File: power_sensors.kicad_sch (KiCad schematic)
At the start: 51 parts, among them U10 MCP6004, U11 MCP6004, U12 ZMPT101B, U13 ZMPT101B, U14 ZMPT101B, U15 JACK_PCB_3.5, U16 JACK_PCB_3.5, U17 JACK_PCB_3.5, U6 MLX91208, U7 MLX91208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

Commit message: Update 3d references and add testpoints
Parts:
- added TP3, TP4, TP5, TP6, TP7, TP8, TP9: (no value), symbol Connector:TestPoint
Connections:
- net 2V5: now also TP3.1
- net at R21.2, U10.10 (+), U14.4 (S1): now also TP6.1
- net at R20.2, U10.5 (+), U13.4 (S1): now also TP5.1
- net at R30.2, U11.10 (+), U17.1 (L)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: now also TP9.1
- net at R28.2, U11.3 (+), U15.1 (L)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: now also TP7.1
- net at R29.2, U11.5 (+), U16.1 (L)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: now also TP8.1
- net at R19.2, U10.3 (+), U12.4 (S1): now also TP4.1
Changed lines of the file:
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@@
   (junction (at 227.33 90.17) (diameter 0) (color 0 0 0 0)
   )
+  (junction (at 160.02 45.72) (diameter 0) (color 0 0 0 0)
+  )
   (junction (at 160.02 86.36) (diameter 0) (color 0 0 0 0)
   )
@@
   (junction (at 52.07 168.91) (diameter 0) (color 0 0 0 0)
   )
+  (junction (at 233.68 46.99) (diameter 0) (color 0 0 0 0)
+  )
   (junction (at 54.61 74.93) (diameter 0) (color 0 0 0 0)
   )
@@
   (junction (at 173.99 93.98) (diameter 0) (color 0 0 0 0)
   )
+  (junction (at 160.02 114.3) (diameter 0) (color 0 0 0 0)
+  )
   (junction (at 31.75 45.72) (diameter 0) (color 0 0 0 0)
   )
@@
   (junction (at 80.01 45.72) (diameter 0) (color 0 0 0 0)
   )
+  (junction (at 233.68 81.28) (diameter 0) (color 0 0 0 0)
+  )
   (junction (at 58.42 116.84) (diameter 0) (color 0 0 0 0)
+  )
+  (junction (at 160.02 80.01) (diameter 0) (color 0 0 0 0)
+  )
+  (junction (at 233.68 114.3) (diameter 0) (color 0 0 0 0)
   )
   (no_connect (at 140.97 177.8))
@@
     (pin "2")
   )
+  (symbol (lib_id "Connector:TestPoint") (at 233.68 114.3 0) (unit 1)
+    (in_bom yes) (on_board yes) (fields_autoplaced)
+    (property "Reference" "TP9" (id 0) (at 236.22 109.7279 0)
+      (effects (font (size 1.27 1.27)) (justify left))
+    )
+    (property "Value" "" (id 1) (at 236.22 112.2679 0)
+      (effects (font (size 1.27 1.27)) (justify left))
+    )
+    (property "Footprint" "" (id 2) (at 238.76 114.3 0)
+      (effects (font (size 1.27 1.27)) hide)
+    )
+    (property "Datasheet" "~" (id 3) (at 238.76 114.3 0)
+      (effects (font (size 1.27 1.27)) hide)
+    )
+    (pin "1")
+  )
   (symbol (lib_id "guille_library:JACK_PCB_3.5") (at 217.17 125.73 0) (unit 1)
     (in_bom yes) (on_board yes) (fields_autoplaced)
@@
     (pin "8")
   )
+  (symbol (lib_id "Connector:TestPoint") (at 160.02 45.72 0) (unit 1)
+    (in_bom yes) (on_board yes) (fields_autoplaced)
+    (property "Reference" "TP4" (id 0) (at 162.56 41.1479 0)
+      (effects (font (size 1.27 1.27)) (justify left))
+    )
+    (property "Value" "" (id 1) (at 162.56 43.6879 0)
+      (effects (font (size 1.27 1.27)) (justify left))
+    )
+    (property "Footprint" "" (id 2) (at 165.1 45.72 0)
+      (effects (font (size 1.27 1.27)) hide)
+    )
+    (property "Datasheet" "~" (id 3) (at 165.1 45.72 0)
+      (effects (font (size 1.27 1.27)) hide)
+    )
+    (pin "1")
+  )
   (symbol (lib_id "power:GND") (at 58.42 92.71 0) (unit 1)
     (in_bom yes) (on_board yes) (fields_autoplaced)
@@
     (pin "1")
     (pin "2")
+  )
+  (symbol (lib_id "Connector:TestPoint") (at 160.02 80.01 0) (unit 1)
+    (in_bom yes) (on_board yes) (fields_autoplaced)
+    (property "Reference" "TP5" (id 0) (at 162.56 75.4379 0)
+      (effects (font (size 1.27 1.27)) (justify left))
+    )
+    (property "Value" "" (id 1) (at 162.56 77.9779 0)
+      (effects (font (size 1.27 1.27)) (justify left))
+    )
+    (property "Footprint" "" (id 2) (at 165.1 80.01 0)
+      (effects (font (size 1.27 1.27)) hide)
+    )
+    (property "Datasheet" "~" (id 3) (at 165.1 80.01 0)
+      (effects (font (size 1.27 1.27)) hide)
+    )
+    (pin "1")
   )
   (symbol (lib_id "Device:R") (at 133.35 93.98 90) (unit 1)
@@
     (pin "2")
   )
+  (symbol (lib_id "Connector:TestPoint") (at 160.02 114.3 0) (unit 1)
+    (in_bom yes) (on_board yes) (fields_autoplaced)
+    (property "Reference" "TP6" (id 0) (at 162.56 109.7279 0)
+      (effects (font (size 1.27 1.27)) (justify left))
+    )
+    (property "Value" "" (id 1) (at 162.56 112.2679 0)
+      (effects (font (size 1.27 1.27)) (justify left))
+    )
+    (property "Footprint" "" (id 2) (at 165.1 114.3 0)
+      (effects (font (size 1.27 1.27)) hide)
+    )
+    (property "Datasheet" "~" (id 3) (at 165.1 114.3 0)
+      (effects (font (size 1.27 1.27)) hide)
+    )
+    (pin "1")
+  )
   (symbol (lib_id "power:GND") (at 69.85 58.42 0) (unit 1)
     (in_bom yes) (on_board yes) (fields_autoplaced)
@@
     )
     (property "Datasheet" "" (id 3) (at 69.85 92.71 0)
+      (effects (font (size 1.27 1.27)) hide)
+    )
+    (pin "1")
+  )
+  (symbol (lib_id "Connector:TestPoint") (at 77.47 171.45 0) (unit 1)
+    (in_bom yes) (on_board yes)
+    (property "Reference" "TP3" (id 0) (at 78.74 163.83 0)
+      (effects (font (size 1.27 1.27)) (justify left))
+    )
+    (property "Value" "" (id 1) (at 78.74 166.37 0)
+      (effects (font (size 1.27 1.27)) (justify left))
+    )
+    (property "Footprint" "" (id 2) (at 82.55 171.45 0)
+      (effects (font (size 1.27 1.27)) hide)
+    )
+    (property "Datasheet" "~" (id 3) (at 82.55 171.45 0)
       (effects (font (size 1.27 1.27)) hide)
     )
@@
     (pin "4")
   )
+  (symbol (lib_id "Connector:TestPoint") (at 233.68 81.28 0) (unit 1)
+    (in_bom yes) (on_board yes) (fields_autoplaced)
+    (property "Reference" "TP8" (id 0) (at 236.22 76.7079 0)
+      (effects (font (size 1.27 1.27)) (justify left))
+    )
+    (property "Value" "" (id 1) (at 236.22 79.2479 0)
+      (effects (font (size 1.27 1.27)) (justify left))
+    )
+    (property "Footprint" "" (id 2) (at 238.76 81.28 0)
+      (effects (font (size 1.27 1.27)) hide)
+    )
+    (property "Datasheet" "~" (id 3) (at 238.76 81.28 0)
+      (effects (font (size 1.27 1.27)) hide)
+    )
+    (pin "1")
+  )
   (symbol (lib_id "power:GND") (at 57.15 109.22 90) (unit 1)
     (in_bom yes) (on_board yes) (fields_autoplaced)
@@
     (pin "2")
   )
+  (symbol (lib_id "Connector:TestPoint") (at 233.68 46.99 0) (unit 1)
+    (in_bom yes) (on_board yes) (fields_autoplaced)
+    (property "Reference" "TP7" (id 0) (at 236.22 42.4179 0)
+      (effects (font (size 1.27 1.27)) (justify left))
+    )
+    (property "Value" "" (id 1) (at 236.22 44.9579 0)
+      (effects (font (size 1.27 1.27)) (justify left))
+    )
+    (property "Footprint" "" (id 2) (at 238.76 46.99 0)
+      (effects (font (size 1.27 1.27)) hide)
+    )
+    (property "Datasheet" "~" (id 3) (at 238.76 46.99 0)
+      (effects (font (size 1.27 1.27)) hide)
+    )
+    (pin "1")
+  )
   (symbol (lib_id "Amplifier_Operational:MCP6004") (at 148.59 162.56 0) (unit 4)

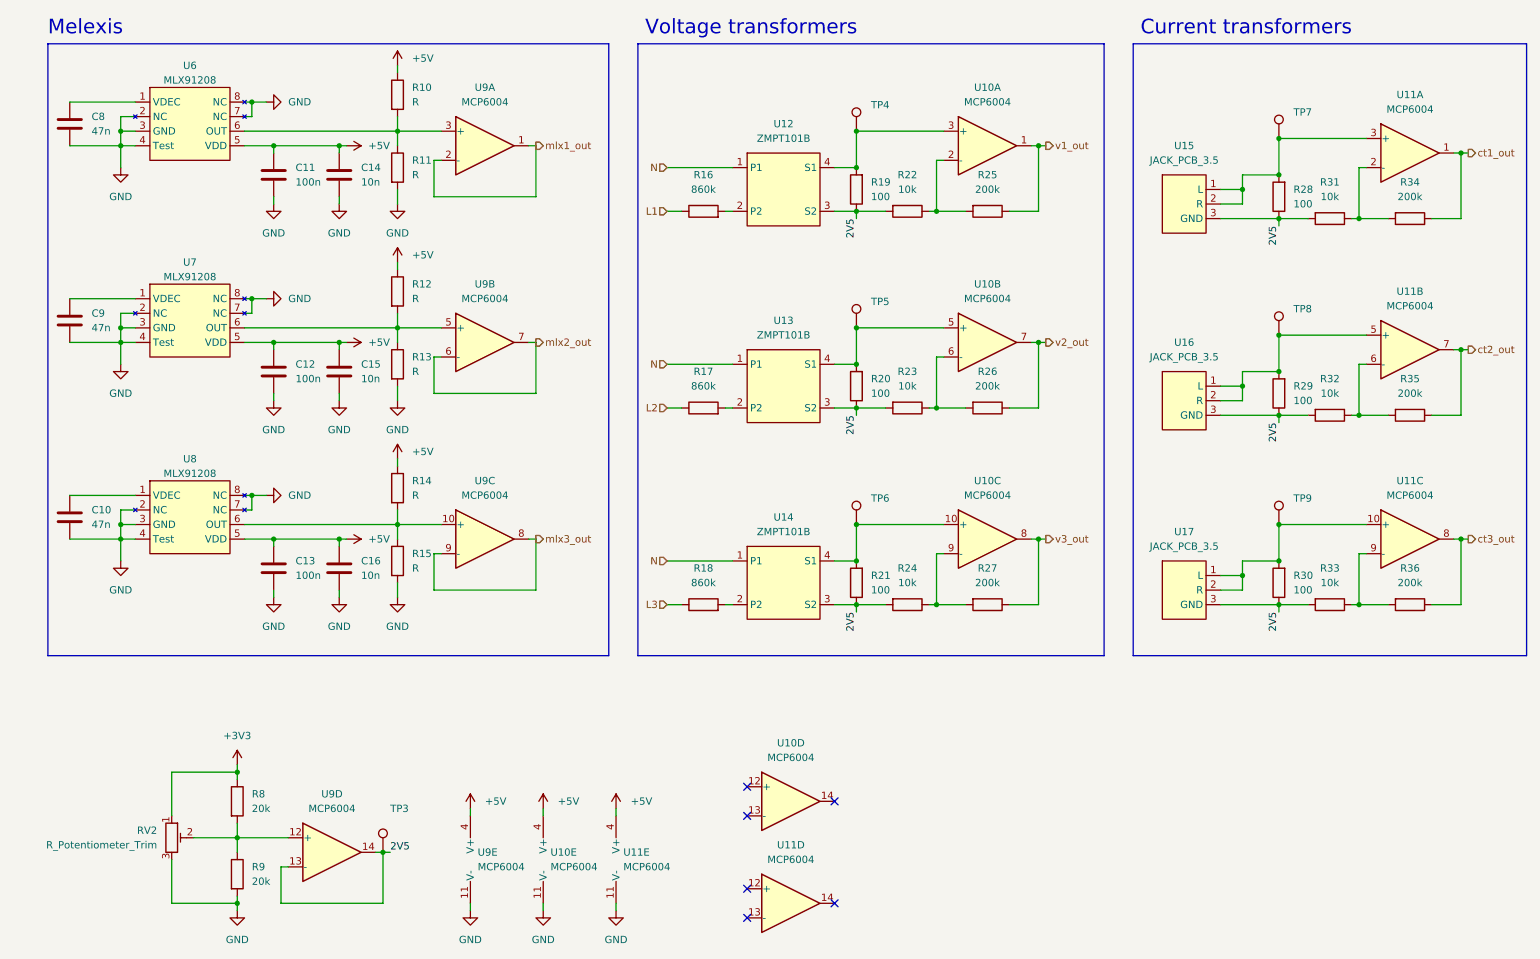
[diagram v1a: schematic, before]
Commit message: Add decoupling capacitors, expansion port and test ponits
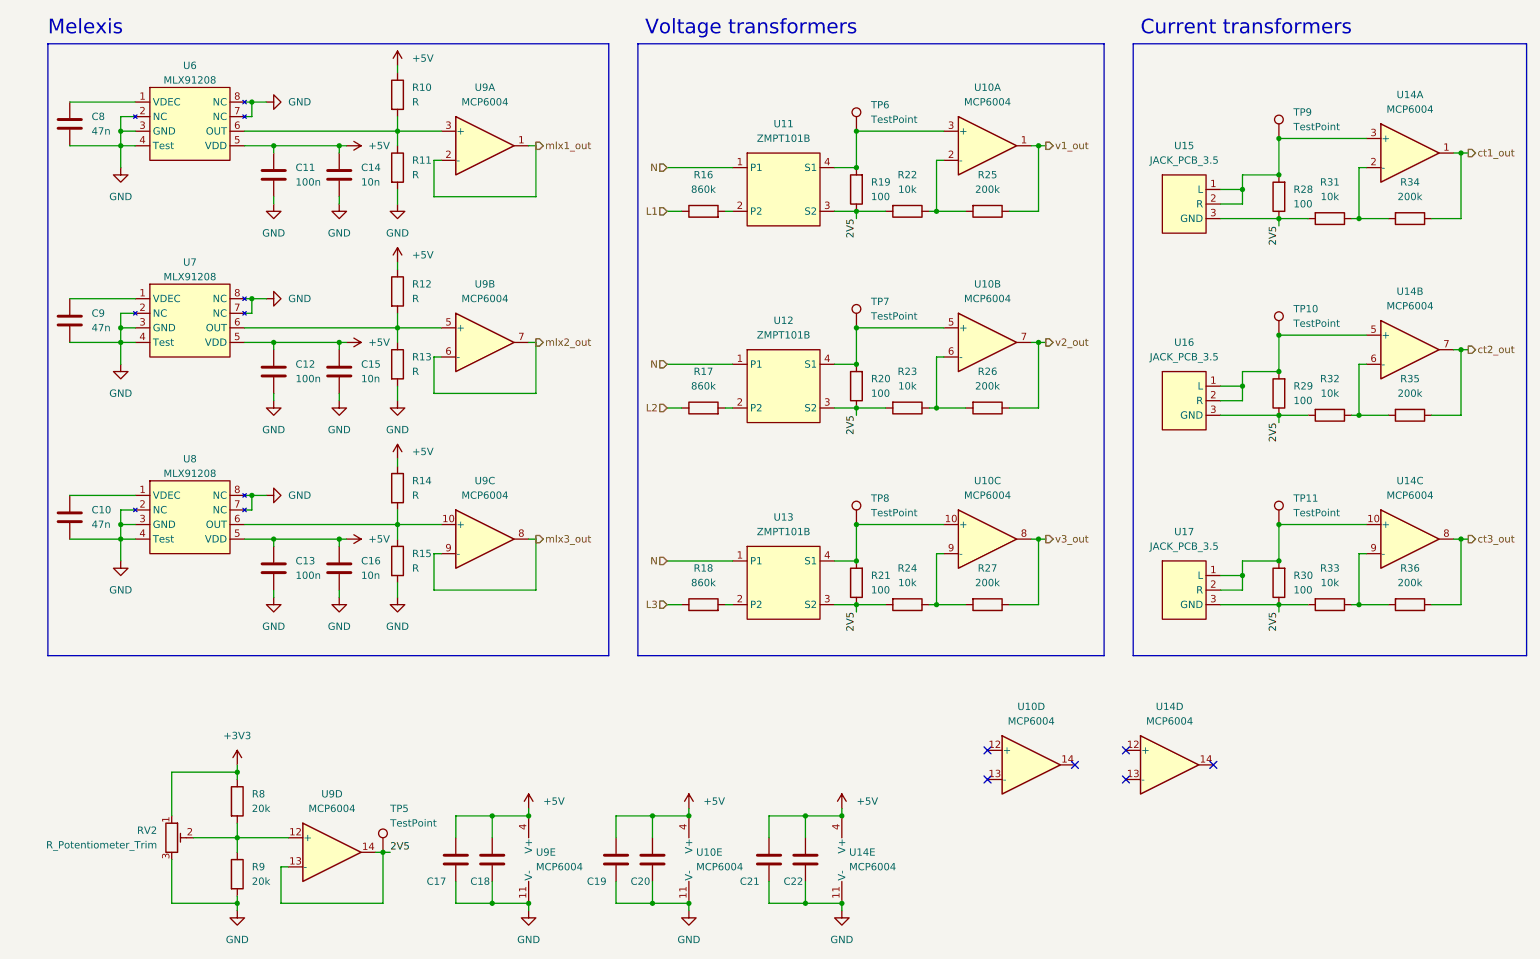
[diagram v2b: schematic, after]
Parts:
- added C17, C18, C19, C20, C21, C22: (no value), symbol Device:C
- TP10: renamed from TP8; value (none) -> TestPoint; footprint (none) -> TestPoint:TestPoint_Pad_D1.5mm
- TP11: renamed from TP9; value (none) -> TestPoint; footprint (none) -> TestPoint:TestPoint_Pad_D1.5mm
- TP5: renamed from TP3; value (none) -> TestPoint; footprint (none) -> TestPoint:TestPoint_Pad_D1.5mm
- TP6: renamed from TP4; value (none) -> TestPoint; footprint (none) -> TestPoint:TestPoint_Pad_D1.5mm
- TP7: renamed from TP5; value (none) -> TestPoint; footprint (none) -> TestPoint:TestPoint_Pad_D1.5mm
- TP8: renamed from TP6; value (none) -> TestPoint; footprint (none) -> TestPoint:TestPoint_Pad_D1.5mm
- TP9: renamed from TP7; value (none) -> TestPoint; footprint (none) -> TestPoint:TestPoint_Pad_D1.5mm
- renumbered U12 to U11, U13 to U12, U14 to U13, U11 to U14
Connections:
- net +5V: now also C17.1, C18.1, C19.1, C20.1, C21.1, C22.1
- net GND: now also C17.2, C18.2, C19.2, C20.2, C21.2, C22.2
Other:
- company: (none) -> Guillermo González Martín
- title: (none) -> Power meter TFM
- moved on the sheet: U10D, U10E, U14D, U14E, U9E

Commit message: Fix divider and leds after board tested
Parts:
- C17, C19, C21: value (none) -> 100n; footprint (none) -> Capacitor_SMD:C_0402_1005Metric
- C18, C20, C22: value (none) -> 1u; footprint (none) -> Capacitor_SMD:C_0402_1005Metric
- R10, R12, R14: value R -> 1,5k
- R11, R13, R15: value R -> 4,6k
- R34, R35, R36: value 200k -> 3,9k
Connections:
- net +5V: no longer R10.1, R12.1, R14.1
- net at R14.2, R15.1, U9.10 (+): no longer U8.6 (OUT)
- net at R10.2, R11.1, U9.3 (+): no longer U6.6 (OUT)
- net at R12.2, R13.1, U9.5 (+): no longer U7.6 (OUT)
- net 2V5 renamed 1V65
- new net: R10.1, U6.6 (OUT)
- new net: R14.1, U8.6 (OUT)
- new net: R12.1, U7.6 (OUT)

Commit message: Last Power Meter 1.0 commit
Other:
- note added: "MAL: EL CONDENSADOR DE 10n VA A OUT"
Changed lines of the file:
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@@
     (effects (font (size 2.54 2.54)) (justify left bottom))
+  )
+  (text "MAL: EL CONDENSADOR DE 10n VA A OUT" (at 60.96 29.21 0)
+    (effects (font (size 1.27 1.27)) (justify left bottom))
   )
   (label "1V65" (at 160.02 95.25 270)
